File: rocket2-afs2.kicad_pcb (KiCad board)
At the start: 2 copper layers, 54 x 54 mm, 51 parts, among them J1 ARM Cortex Debug, J3 XT60 POWER, U1 STM32F105RCT6, U2 LD1086DT33TR, U4 USBLC6-2SC6, U5 ADXL383, Y1 8MHz

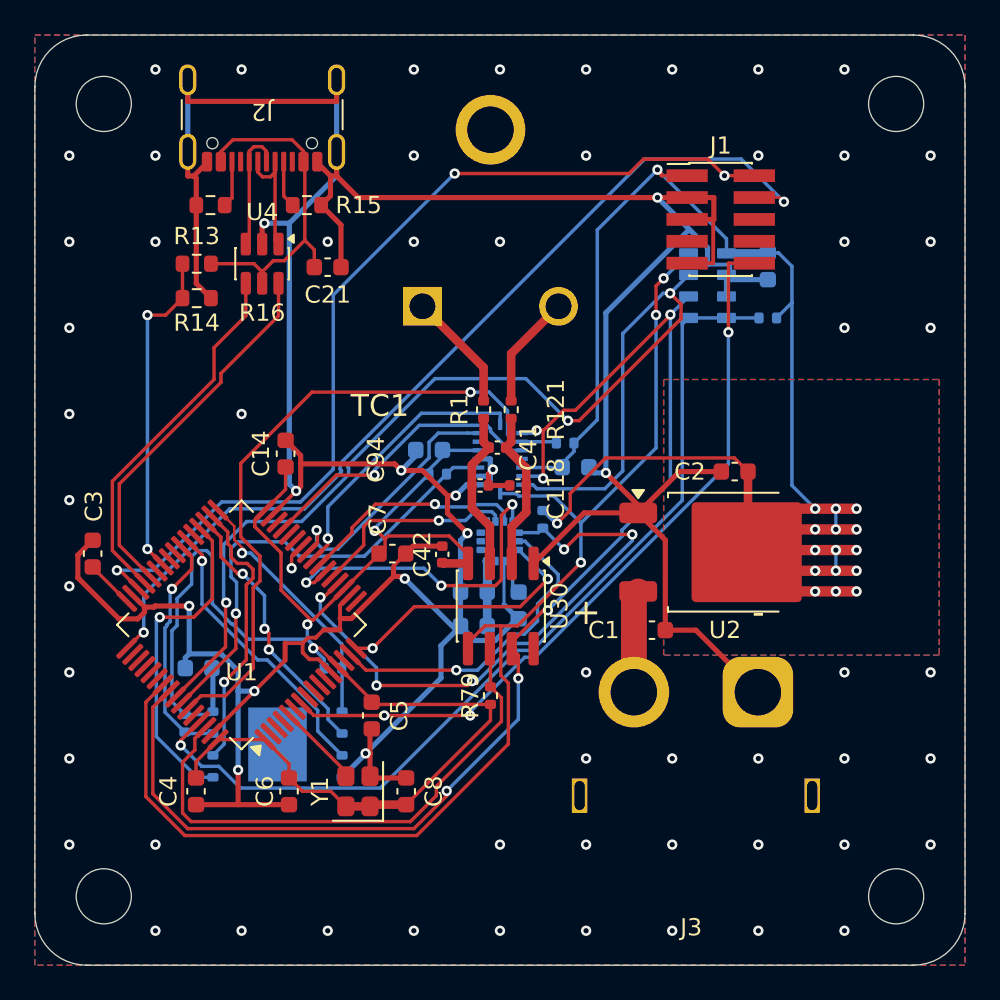
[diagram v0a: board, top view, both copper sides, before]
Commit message: Finished routing iteration 1. Going to try moving everything to the front next
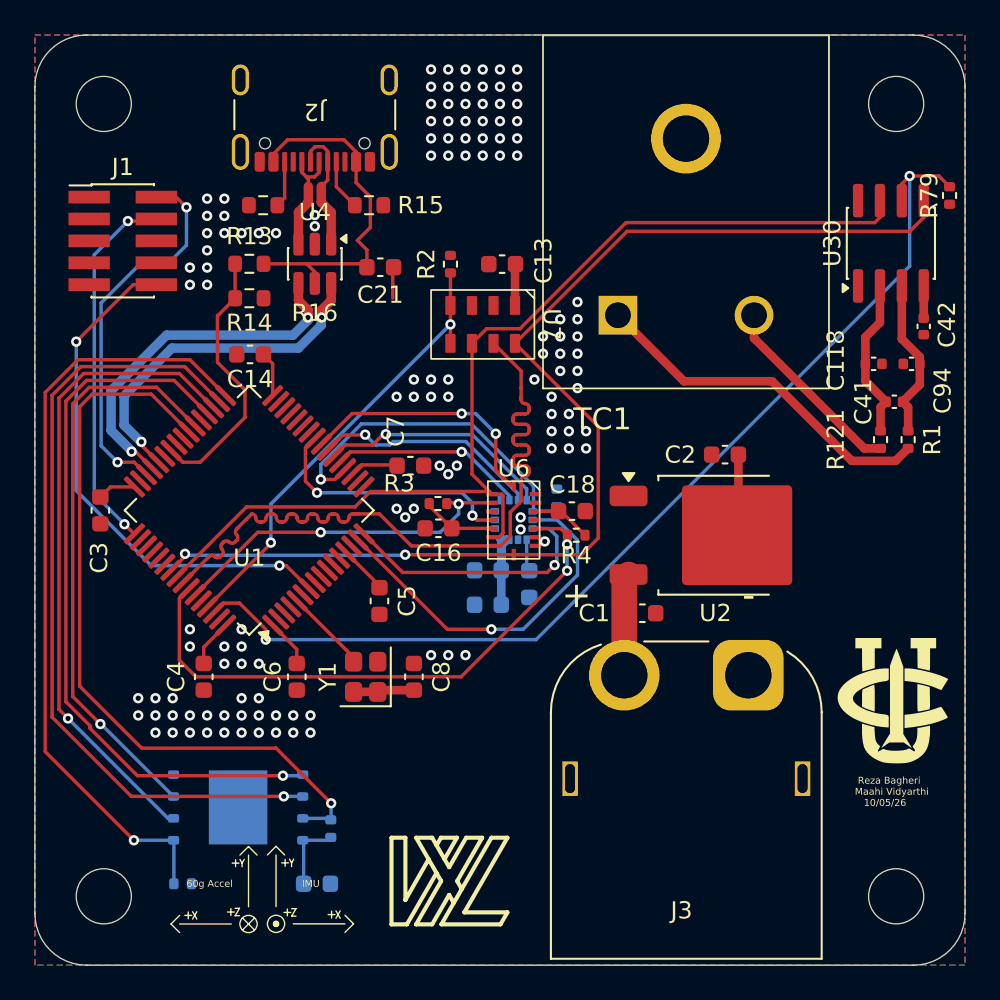
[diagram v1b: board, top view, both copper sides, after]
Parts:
- added REF**: UCIRP_Logo_1, 0UCIRP-KiCAD-Lib:UCIRP_Logo_1, F.Cu at (148.0, 136.5)
- C13, C16, C18, R2, R3, R4, U6, U7: moved to F.Cu
- moved R79 39.4 mm to (151.1, 107.3)
- moved J1 34.7 mm to (103.1, 110.0)
- moved C42 30.9 mm to (149.6, 114.9), turned to -90 degrees
- moved U30 30.9 mm to (147.7, 110.1), turned to 90 degrees
- moved C94 26.0 mm to (148.9, 117.1), turned to 180 degrees
- moved R1 24.7 mm to (148.7, 121.5), turned to 90 degrees
- moved C41 23.2 mm to (147.9, 119.3), turned to 180 degrees
- moved C118 21.8 mm to (146.7, 117.1), turned to 180 degrees
- moved R121 21.5 mm to (147.1, 121.5), turned to 90 degrees
- moved R2 18.7 mm to (122.1, 111.3), turned to -90 degrees
- moved C13 15.4 mm to (125.1, 111.3), turned to 180 degrees
- moved R5 15.3 mm to (106.6, 147.3), turned to 180 degrees
- moved C12 14.3 mm to (114.4, 147.3), turned to 0 degrees
- moved U7 13.2 mm to (124.0, 114.8), turned to -90 degrees
- moved TC1 11.4 mm to (135.8, 108.3)
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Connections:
- J2 pad S1: GND -> (no net)
- U1 pad 25: /IMU_INT2 -> /IMU_INT3
- U1 pad 26: /IMU_INT3 -> unconnected-(U1-PB0-Pad26)
- U1 pad 29: /IMU_INT4 -> unconnected-(U1-PB10-Pad29)
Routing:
- net GND: track 268.6 -> 2.00 mm, vias 69 -> 127
- net +3.3V: track 214.4 -> 46.8 mm, vias 20 -> 0
- net /SWDCLK: track 54.4 -> 21.6 mm
- net /SWDIO: track 54.9 -> 22.2 mm, vias 3 -> 2
- net /MEM_SCK: track 16.2 -> 46.4 mm
- net /MEM_~{HOLD}: track 13.8 -> 43.8 mm
- net /MEM_~{CS}: track 15.1 -> 45.1 mm
- net /TC_~{CS}: track 31.5 -> 60.3 mm, vias 0 -> 2
- net /ALT_~{CS}: track 53.7 -> 26.3 mm, vias 1 -> 2
- net /IMU_ALT_TC_MOSI: track 65.8 -> 42.1 mm, vias 3 -> 0
- net /MEM_MOSI: track 19.2 -> 42.6 mm
- net /MEM_MISO: track 15.7 -> 37.7 mm, vias 3 -> 1
- net /IMU_ACCEL_~{CS}: track 39.4 -> 20.5 mm, vias 1 -> 2
- net /IMU_INT4: track 17.2 -> 0.00 mm, vias 1 -> 0
- net /MEM_~{WP}: track 16.5 -> 33.7 mm
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- removed copper zone on B.Cu, net +3.3V
- removed copper zone on F.Cu, net +3.3V
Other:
- board text added: "60g Accel"
- board text added: "IMU"
- board text added: "Reza Bagheri Maahi Vidyarthi 10/05/26"

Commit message: Moved all to front
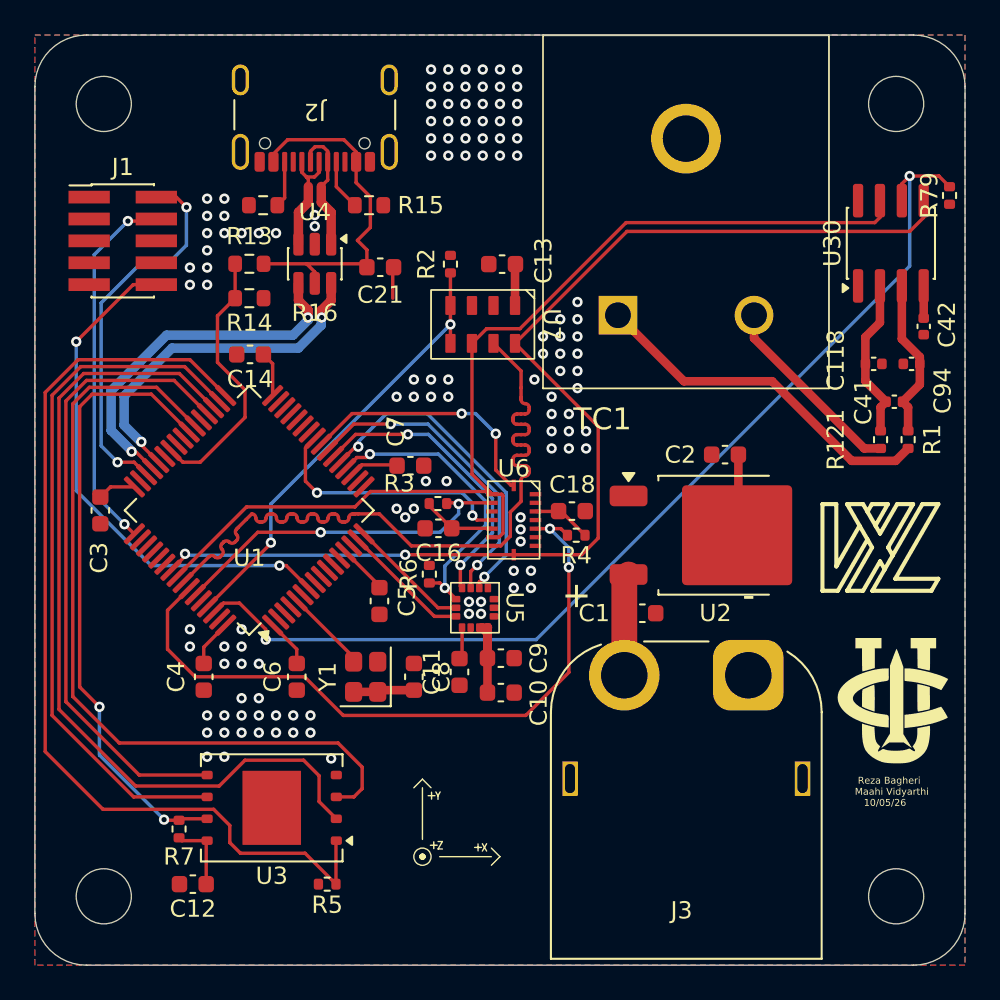
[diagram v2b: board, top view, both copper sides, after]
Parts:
- C10, C11, C12, C9, R5, R6, R7, U3, U5: moved to F.Cu
- moved R7 8.81 mm to (106.4, 144.1)
- moved R6 8.62 mm to (120.9, 129.3)
- moved R5 8.39 mm to (115.0, 147.3), turned to 0 degrees
- moved C12 7.21 mm to (107.2, 147.3), turned to 180 degrees
- moved C11 6.51 mm to (122.6, 135.0)
- moved U5 5.57 mm to (123.5, 131.2)
- moved C10 5.15 mm to (125.0, 136.2), turned to 0 degrees
- moved C9 5.15 mm to (125.0, 134.2), turned to 0 degrees
- moved U3 1.95 mm to (111.8, 142.9), turned to 180 degrees
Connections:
- U1 pad 15: /ACCEL_INT0 -> /ACCEL_INT1
- U1 pad 16: /ACCEL_INT1 -> /ACCEL_INT0
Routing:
- net /ACCEL_INT0: track 21.3 -> 7.12 mm, vias 1 -> 0
- net /MEM_~{WP}: track 33.7 -> 46.9 mm, vias 1 -> 0
- net /MEM_MISO: track 37.7 -> 49.3 mm, vias 1 -> 0
- net /MEM_~{CS}: track 45.1 -> 56.2 mm, vias 1 -> 0
- net /ACCEL_INT1: track 15.5 -> 7.54 mm, vias 1 -> 0
- net /MEM_~{HOLD}: track 43.8 -> 36.1 mm, vias 1 -> 2
- net /ACCEL_SCK: track 11.4 -> 19.1 mm, vias 1 -> 2
- net /IMU_GYRO_~{CS}: track 33.9 -> 40.8 mm
- net /MEM_MOSI: track 42.6 -> 36.9 mm, vias 1 -> 0
- net /MEM_SCK: track 46.4 -> 40.8 mm, vias 1 -> 0
- net /ACCEL_MOSI: track 13.4 -> 18.4 mm, vias 1 -> 2
- net /ACCEL_MISO: track 13.7 -> 17.3 mm, vias 1 -> 2
- net /ACCEL_~{CS}: track 20.4 -> 17.6 mm, vias 1 -> 2
- net GND: vias 127 -> 124
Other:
- board text removed: "60g Accel"
- board text removed: "IMU"
